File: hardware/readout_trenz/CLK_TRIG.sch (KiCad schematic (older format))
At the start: 11 parts, among them J2 Conn_Coaxial, J3 Conn_Coaxial, U1 NLSV4T244E, U2 LM6321N, U3 LM6321N

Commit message: _
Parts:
- removed U2, U3: LM6321N, Package_DIP:DIP-8_W7.62mm, symbol Amplifier_Buffer:LM6321N
- C1, C2: footprint (none) -> Capacitor_SMD:C_0603_1608Metric_Pad1.05x0.95mm_HandSolder
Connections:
- net labels removed: +3.3V
- wire segments 35 -> 29
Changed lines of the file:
@@
 Comment4 ""
 $EndDescr
-$Comp
-L Amplifier_Buffer:LM6321N U2
-U 1 1 60C7627C
-P 15300 2450
-F 0 "U2" H 15644 2496 50  0000 L CNN
-F 1 "LM6321N" H 15644 2405 50  0000 L CNN
-F 2 "Package_DIP:DIP-8_W7.62mm" H 15500 2050 50  0001 C CNN
-F 3 "http://www.electronica60norte.com/mwfls/pdf/LM6221.pdf" H 15300 2450 50  0001 C CNN
-	1    15300 2450
-	1    0    0    -1
-$EndComp
-$Comp
-L power:+3.3V #PWR08
-U 1 1 60C78956
-P 15200 1950
-F 0 "#PWR08" H 15200 1800 50  0001 C CNN
-F 1 "+3.3V" H 15215 2123 50  0000 C CNN
-F 2 "" H 15200 1950 50  0001 C CNN
-F 3 "" H 15200 1950 50  0001 C CNN
-	1    15200 1950
-	1    0    0    -1
-$EndComp
-Wire Wire Line
-	14000 2450 15000 2450
 Wire Wire Line
 	6850 3350 7750 3350
-Wire Wire Line
-	15200 2750 15200 2950
-Wire Wire Line
-	15200 2150 15200 1950
 Text HLabel 7750 3350 2    50   Output ~ 0
 CLOCK
@@
 	1    0    0    -1
 $EndComp
-$Comp
-L Amplifier_Buffer:LM6321N U3
-U 1 1 60C7B23A
-P 15300 4450
-F 0 "U3" H 15644 4496 50  0000 L CNN
-F 1 "LM6321N" H 15644 4405 50  0000 L CNN
-F 2 "Package_DIP:DIP-8_W7.62mm" H 15500 4050 50  0001 C CNN
-F 3 "http://www.electronica60norte.com/mwfls/pdf/LM6221.pdf" H 15300 4450 50  0001 C CNN
-	1    15300 4450
-	1    0    0    -1
-$EndComp
-$Comp
-L power:+3.3V #PWR010
-U 1 1 60C7B262
-P 15200 3950
-F 0 "#PWR010" H 15200 3800 50  0001 C CNN
-F 1 "+3.3V" H 15215 4123 50  0000 C CNN
-F 2 "" H 15200 3950 50  0001 C CNN
-F 3 "" H 15200 3950 50  0001 C CNN
-	1    15200 3950
-	1    0    0    -1
-$EndComp
 Wire Wire Line
 	4500 4200 4500 4500
@@
 	4700 4000 5500 4000
 Wire Wire Line
-	14000 4450 15000 4450
-Wire Wire Line
 	6850 3650 7750 3650
 Wire Wire Line
 	5500 4300 5500 4500
-Wire Wire Line
-	15200 4750 15200 4950
-Wire Wire Line
-	15200 4150 15200 3950
 Text HLabel 7750 3650 2    50   Output ~ 0
 TRIGGER
 Text Notes 4000 4000 0    50   ~ 0
 TRIGGER
-$Comp
-L power:GNDD #PWR09
-U 1 1 613569FF
-P 15200 2950
-F 0 "#PWR09" H 15200 2700 50  0001 C CNN
-F 1 "GNDD" H 15204 2795 50  0000 C CNN
-F 2 "" H 15200 2950 50  0001 C CNN
-F 3 "" H 15200 2950 50  0001 C CNN
-	1    15200 2950
-	1    0    0    -1
-$EndComp
 $Comp
 L power:GNDD #PWR03
@@
 F 3 "" H 5500 4500 50  0001 C CNN
 	1    5500 4500
-	1    0    0    -1
-$EndComp
-$Comp
-L power:GNDD #PWR011
-U 1 1 61358963
-P 15200 4950
-F 0 "#PWR011" H 15200 4700 50  0001 C CNN
-F 1 "GNDD" H 15204 4795 50  0000 C CNN
-F 2 "" H 15200 4950 50  0001 C CNN
-F 3 "" H 15200 4950 50  0001 C CNN
-	1    15200 4950
 	1    0    0    -1
 $EndComp
@@
 F 0 "C2" V 6900 2550 50  0000 L CNN
 F 1 "0.1uF" V 6800 2500 50  0000 L CNN
-F 2 "" H 6700 2600 50  0001 C CNN
+F 2 "Capacitor_SMD:C_0603_1608Metric_Pad1.05x0.95mm_HandSolder" H 6700 2600 50  0001 C CNN
 F 3 "~" H 6700 2600 50  0001 C CNN
 	1    6700 2600
@@
 F 0 "C1" V 6500 2550 50  0000 L CNN
 F 1 "0.1uF" V 6400 2500 50  0000 L CNN
-F 2 "" H 6300 2600 50  0001 C CNN
+F 2 "Capacitor_SMD:C_0603_1608Metric_Pad1.05x0.95mm_HandSolder" H 6300 2600 50  0001 C CNN
 F 3 "~" H 6300 2600 50  0001 C CNN
 	1    6300 2600

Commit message: Readout Preliminary Schematic Made
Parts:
- U1: footprint (none) -> Package_SO:TSSOP-14_4.4x5mm_P0.65mm; Item Cost (none) -> $1.97; MFN (none) -> NLSV4T244EDTR2G; Manufacturer (none) -> ON Semiconductors; Supplier (none) -> Digi-Key; Supplier P/N (none) -> NLSV4T244EDTR2GOSCT-ND
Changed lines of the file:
@@
 F 0 "U1" H 6500 3975 50  0000 C CNN
 F 1 "NLSV4T244E" H 6500 3884 50  0000 C CNN
-F 2 "" H 6500 3500 50  0001 C CNN
+F 2 "Package_SO:TSSOP-14_4.4x5mm_P0.65mm" H 6500 3500 50  0001 C CNN
 F 3 "https://www.onsemi.com/pdf/datasheet/nlsv4t244e-d.pdf" H 6500 3500 50  0001 C CNN
+F 4 "$1.97" H 6500 3500 50  0001 C CNN "Item Cost"
+F 5 "NLSV4T244EDTR2G" H 6500 3500 50  0001 C CNN "MFN"
+F 6 "ON Semiconductors" H 6500 3500 50  0001 C CNN "Manufacturer"
+F 7 "Digi-Key" H 6500 3500 50  0001 C CNN "Supplier"
+F 8 "NLSV4T244EDTR2GOSCT-ND" H 6500 3500 50  0001 C CNN "Supplier P/N"
 	1    6500 3500
 	1    0    0    -1

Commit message: Footprints Assigned
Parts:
- J2, J3: footprint (none) -> Readout_Board_Parts:lemo-EPB.00.250.NTN
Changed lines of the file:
@@
 F 0 "J3" H 4428 4238 50  0000 C CNN
 F 1 "Conn_Coaxial" H 4428 4147 50  0000 C CNN
-F 2 "" H 4500 4000 50  0001 C CNN
+F 2 "Readout_Board_Parts:lemo-EPB.00.250.NTN" H 4500 4000 50  0001 C CNN
 F 3 " ~" H 4500 4000 50  0001 C CNN
 	1    4500 4000
@@
 F 0 "J2" H 4428 3238 50  0000 C CNN
 F 1 "Conn_Coaxial" H 4428 3147 50  0000 C CNN
-F 2 "" H 4500 3000 50  0001 C CNN
+F 2 "Readout_Board_Parts:lemo-EPB.00.250.NTN" H 4500 3000 50  0001 C CNN
 F 3 " ~" H 4500 3000 50  0001 C CNN
 	1    4500 3000

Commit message: Starting Layout
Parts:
- C1, C2: Item Cost (none) -> $0.1; MFN (none) -> 885012206046; Manufacturer (none) -> Würth Elektronik; Supplier  (none) -> Digi-Key; Supplier P/N (none) -> 732-7965-1-ND
- U1: footprint Package_SO:TSSOP-14_4.4x5mm_P0.65mm -> Package_SO:SOIC-14_3.9x8.7mm_P1.27mm
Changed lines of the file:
@@
 F 0 "U1" H 6500 3975 50  0000 C CNN
 F 1 "NLSV4T244E" H 6500 3884 50  0000 C CNN
-F 2 "Package_SO:TSSOP-14_4.4x5mm_P0.65mm" H 6500 3500 50  0001 C CNN
+F 2 "Package_SO:SOIC-14_3.9x8.7mm_P1.27mm" H 6500 3500 50  0001 C CNN
 F 3 "https://www.onsemi.com/pdf/datasheet/nlsv4t244e-d.pdf" H 6500 3500 50  0001 C CNN
 F 4 "$1.97" H 6500 3500 50  0001 C CNN "Item Cost"
@@
 F 1 "0.1uF" V 6800 2500 50  0000 L CNN
 F 2 "Capacitor_SMD:C_0603_1608Metric_Pad1.05x0.95mm_HandSolder" H 6700 2600 50  0001 C CNN
-F 3 "~" H 6700 2600 50  0001 C CNN
+F 3 "https://www.we-online.de/katalog/datasheet/885012206046.pdf" H 6700 2600 50  0001 C CNN
+F 4 "$0.1" H 6700 2600 50  0001 C CNN "Item Cost"
+F 5 "885012206046" H 6700 2600 50  0001 C CNN "MFN"
+F 6 "Würth Elektronik" H 6700 2600 50  0001 C CNN "Manufacturer"
+F 7 "Digi-Key" H 6700 2600 50  0001 C CNN "Supplier "
+F 8 "732-7965-1-ND" H 6700 2600 50  0001 C CNN "Supplier P/N"
 	1    6700 2600
 	0    -1   -1   0
@@
 F 1 "0.1uF" V 6400 2500 50  0000 L CNN
 F 2 "Capacitor_SMD:C_0603_1608Metric_Pad1.05x0.95mm_HandSolder" H 6300 2600 50  0001 C CNN
-F 3 "~" H 6300 2600 50  0001 C CNN
+F 3 "https://www.we-online.de/katalog/datasheet/885012206046.pdf" H 6300 2600 50  0001 C CNN
+F 4 "$0.1" H 6300 2600 50  0001 C CNN "Item Cost"
+F 5 "885012206046" H 6300 2600 50  0001 C CNN "MFN"
+F 6 "Würth Elektronik" H 6300 2600 50  0001 C CNN "Manufacturer"
+F 7 "Digi-Key" H 6300 2600 50  0001 C CNN "Supplier "
+F 8 "732-7965-1-ND" H 6300 2600 50  0001 C CNN "Supplier P/N"
 	1    6300 2600
 	0    -1   -1   0

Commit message: -
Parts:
- J2, J3: footprint Readout_Board_Parts:lemo-EPB.00.250.NTN -> readout_trenz:lemo-EPB.00.250.NTN
- R1, R2: value 50 -> 56; Item Cost (none) -> $0.1; MFN (none) -> CRCW060356R0FKEAC; Manufacturer (none) -> Vishay Dale; Supplier  (none) -> Digi-Key; Supplier P/N (none) -> 541-5483-1-ND
- R3, R4: Item Cost (none) -> $0.01; MFN (none) -> CR0603AFX-1000ELF; Manufacturer (none) -> Bourns Inc.; Supplier  (none) -> Digi-Key; Supplier P/N (none) -> 118-CR0603AFX-1000ELFCT-ND
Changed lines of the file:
@@
 F 0 "J3" H 4428 4238 50  0000 C CNN
 F 1 "Conn_Coaxial" H 4428 4147 50  0000 C CNN
-F 2 "Readout_Board_Parts:lemo-EPB.00.250.NTN" H 4500 4000 50  0001 C CNN
+F 2 "readout_trenz:lemo-EPB.00.250.NTN" H 4500 4000 50  0001 C CNN
 F 3 " ~" H 4500 4000 50  0001 C CNN
 	1    4500 4000
@@
 P 5500 4150
 F 0 "R2" H 5570 4196 50  0000 L CNN
-F 1 "50" H 5570 4105 50  0000 L CNN
+F 1 "56" H 5570 4105 50  0000 L CNN
 F 2 "Resistor_SMD:R_0603_1608Metric_Pad1.05x0.95mm_HandSolder" V 5430 4150 50  0001 C CNN
-F 3 "~" H 5500 4150 50  0001 C CNN
+F 3 "https://www.vishay.com/docs/28773/crcwce3.pdf" H 5500 4150 50  0001 C CNN
+F 4 "$0.1" H 5500 4150 50  0001 C CNN "Item Cost"
+F 5 "CRCW060356R0FKEAC" H 5500 4150 50  0001 C CNN "MFN"
+F 6 "Vishay Dale" H 5500 4150 50  0001 C CNN "Manufacturer"
+F 7 "Digi-Key" H 5500 4150 50  0001 C CNN "Supplier "
+F 8 "541-5483-1-ND" H 5500 4150 50  0001 C CNN "Supplier P/N"
 	1    5500 4150
 	1    0    0    -1
@@
 P 5500 3150
 F 0 "R1" H 5570 3196 50  0000 L CNN
-F 1 "50" H 5570 3105 50  0000 L CNN
+F 1 "56" H 5570 3105 50  0000 L CNN
 F 2 "Resistor_SMD:R_0603_1608Metric_Pad1.05x0.95mm_HandSolder" V 5430 3150 50  0001 C CNN
-F 3 "~" H 5500 3150 50  0001 C CNN
+F 3 "https://www.vishay.com/docs/28773/crcwce3.pdf" H 5500 3150 50  0001 C CNN
+F 4 "$0.1" H 5500 3150 50  0001 C CNN "Item Cost"
+F 5 "CRCW060356R0FKEAC" H 5500 3150 50  0001 C CNN "MFN"
+F 6 "Vishay Dale" H 5500 3150 50  0001 C CNN "Manufacturer"
+F 7 "Digi-Key" H 5500 3150 50  0001 C CNN "Supplier "
+F 8 "541-5483-1-ND" H 5500 3150 50  0001 C CNN "Supplier P/N"
 	1    5500 3150
 	1    0    0    -1
@@
 F 0 "J2" H 4428 3238 50  0000 C CNN
 F 1 "Conn_Coaxial" H 4428 3147 50  0000 C CNN
-F 2 "Readout_Board_Parts:lemo-EPB.00.250.NTN" H 4500 3000 50  0001 C CNN
+F 2 "readout_trenz:lemo-EPB.00.250.NTN" H 4500 3000 50  0001 C CNN
 F 3 " ~" H 4500 3000 50  0001 C CNN
 	1    4500 3000
@@
 F 1 "100" H 6070 3755 50  0000 L CNN
 F 2 "Resistor_SMD:R_0603_1608Metric_Pad1.05x0.95mm_HandSolder" V 5930 3800 50  0001 C CNN
-F 3 "~" H 6000 3800 50  0001 C CNN
+F 3 "https://www.bourns.com/docs/product-datasheets/crxxxxa.pdf" H 6000 3800 50  0001 C CNN
+F 4 "$0.01" H 6000 3800 50  0001 C CNN "Item Cost"
+F 5 "CR0603AFX-1000ELF" H 6000 3800 50  0001 C CNN "MFN"
+F 6 "Bourns Inc." H 6000 3800 50  0001 C CNN "Manufacturer"
+F 7 "Digi-Key" H 6000 3800 50  0001 C CNN "Supplier "
+F 8 "118-CR0603AFX-1000ELFCT-ND" H 6000 3800 50  0001 C CNN "Supplier P/N"
 	1    6000 3800
 	-1   0    0    -1
@@
 F 1 "100" H 6070 3155 50  0000 L CNN
 F 2 "Resistor_SMD:R_0603_1608Metric_Pad1.05x0.95mm_HandSolder" V 5930 3200 50  0001 C CNN
-F 3 "~" H 6000 3200 50  0001 C CNN
+F 3 "https://www.bourns.com/docs/product-datasheets/crxxxxa.pdf" H 6000 3200 50  0001 C CNN
+F 4 "$0.01" H 6000 3200 50  0001 C CNN "Item Cost"
+F 5 "CR0603AFX-1000ELF" H 6000 3200 50  0001 C CNN "MFN"
+F 6 "Bourns Inc." H 6000 3200 50  0001 C CNN "Manufacturer"
+F 7 "Digi-Key" H 6000 3200 50  0001 C CNN "Supplier "
+F 8 "118-CR0603AFX-1000ELFCT-ND" H 6000 3200 50  0001 C CNN "Supplier P/N"
 	1    6000 3200
 	-1   0    0    -1

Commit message: On Layout
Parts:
- U1: footprint Package_SO:SOIC-14_3.9x8.7mm_P1.27mm -> Package_SO:TSSOP-14_4.4x5mm_P0.65mm; Supplier  (none) -> Digi-Key
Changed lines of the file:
@@
 F 0 "U1" H 6500 3975 50  0000 C CNN
 F 1 "NLSV4T244E" H 6500 3884 50  0000 C CNN
-F 2 "Package_SO:SOIC-14_3.9x8.7mm_P1.27mm" H 6500 3500 50  0001 C CNN
+F 2 "Package_SO:TSSOP-14_4.4x5mm_P0.65mm" H 6500 3500 50  0001 C CNN
 F 3 "https://www.onsemi.com/pdf/datasheet/nlsv4t244e-d.pdf" H 6500 3500 50  0001 C CNN
 F 4 "$1.97" H 6500 3500 50  0001 C CNN "Item Cost"
@@
 F 7 "Digi-Key" H 6500 3500 50  0001 C CNN "Supplier"
 F 8 "NLSV4T244EDTR2GOSCT-ND" H 6500 3500 50  0001 C CNN "Supplier P/N"
+F 9 "Digi-Key" H 6500 3500 50  0001 C CNN "Supplier "
 	1    6500 3500
 	1    0    0    -1

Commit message: Readout Layout Started
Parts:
- U1: Supplier Digi-Key -> (none)
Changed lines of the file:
@@
 F 5 "NLSV4T244EDTR2G" H 6500 3500 50  0001 C CNN "MFN"
 F 6 "ON Semiconductors" H 6500 3500 50  0001 C CNN "Manufacturer"
-F 7 "Digi-Key" H 6500 3500 50  0001 C CNN "Supplier"
+F 7 "" H 6500 3500 50  0001 C CNN "Supplier"
 F 8 "NLSV4T244EDTR2GOSCT-ND" H 6500 3500 50  0001 C CNN "Supplier P/N"
 F 9 "Digi-Key" H 6500 3500 50  0001 C CNN "Supplier "

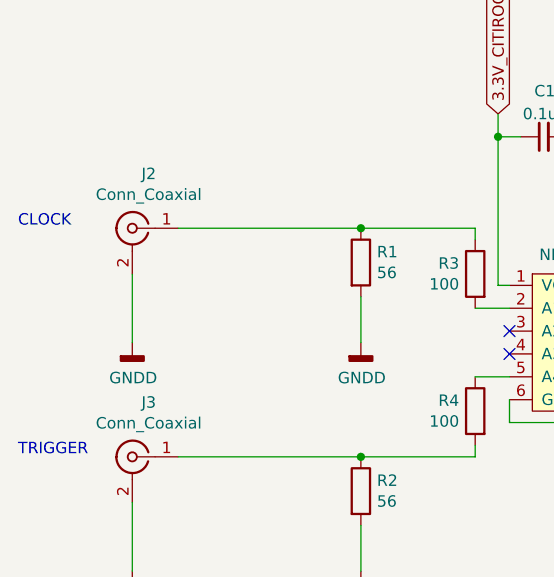
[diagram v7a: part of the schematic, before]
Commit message: Netlist errors fixed
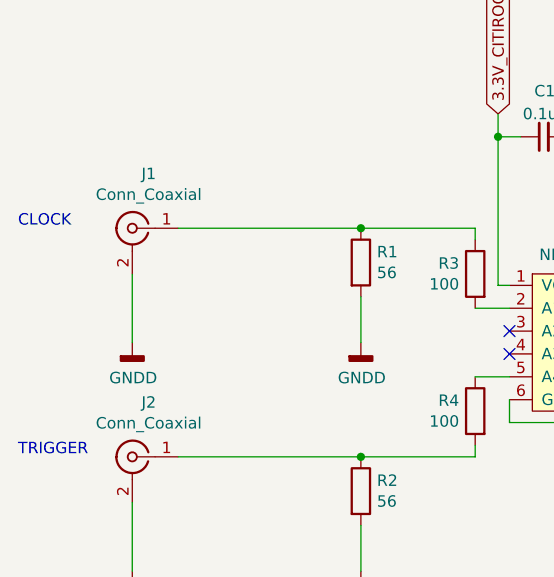
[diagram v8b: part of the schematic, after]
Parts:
- renumbered J2 to J1, J3 to J2
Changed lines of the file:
@@
 CLOCK\n
 $Comp
-L Connector:Conn_Coaxial J3
+L Connector:Conn_Coaxial J2
 U 1 1 60C7B226
 P 4500 4000
-F 0 "J3" H 4428 4238 50  0000 C CNN
+F 0 "J2" H 4428 4238 50  0000 C CNN
 F 1 "Conn_Coaxial" H 4428 4147 50  0000 C CNN
 F 2 "readout_trenz:lemo-EPB.00.250.NTN" H 4500 4000 50  0001 C CNN
@@
 TRIGGER
 $Comp
-L power:GNDD #PWR03
+L power:GNDD #PWR02
 U 1 1 6135894F
 P 4500 4500
-F 0 "#PWR03" H 4500 4250 50  0001 C CNN
+F 0 "#PWR02" H 4500 4250 50  0001 C CNN
 F 1 "GNDD" H 4504 4345 50  0000 C CNN
 F 2 "" H 4500 4500 50  0001 C CNN
@@
 $EndComp
 $Comp
-L power:GNDD #PWR05
+L power:GNDD #PWR04
 U 1 1 61358959
 P 5500 4500
-F 0 "#PWR05" H 5500 4250 50  0001 C CNN
+F 0 "#PWR04" H 5500 4250 50  0001 C CNN
 F 1 "GNDD" H 5504 4345 50  0000 C CNN
 F 2 "" H 5500 4500 50  0001 C CNN
@@
 	6850 3850 6850 3750
 $Comp
-L power:GNDD #PWR07
+L power:GNDD #PWR06
 U 1 1 61480617
 P 6500 3850
-F 0 "#PWR07" H 6500 3600 50  0001 C CNN
+F 0 "#PWR06" H 6500 3600 50  0001 C CNN
 F 1 "GNDD" H 6504 3695 50  0000 C CNN
 F 2 "" H 6500 3850 50  0001 C CNN
@@
 	6100 3250 6150 3250
 $Comp
-L power:GNDD #PWR04
+L power:GNDD #PWR03
 U 1 1 613558E3
 P 5500 3500
-F 0 "#PWR04" H 5500 3250 50  0001 C CNN
+F 0 "#PWR03" H 5500 3250 50  0001 C CNN
 F 1 "GNDD" H 5504 3345 50  0000 C CNN
 F 2 "" H 5500 3500 50  0001 C CNN
@@
 $EndComp
 $Comp
-L power:GNDD #PWR02
+L power:GNDD #PWR01
 U 1 1 6135534F
 P 4500 3500
-F 0 "#PWR02" H 4500 3250 50  0001 C CNN
+F 0 "#PWR01" H 4500 3250 50  0001 C CNN
 F 1 "GNDD" H 4504 3345 50  0000 C CNN
 F 2 "" H 4500 3500 50  0001 C CNN
@@
 $EndComp
 $Comp
-L Connector:Conn_Coaxial J2
+L Connector:Conn_Coaxial J1
 U 1 1 60C74CEF
 P 4500 3000
-F 0 "J2" H 4428 3238 50  0000 C CNN
+F 0 "J1" H 4428 3238 50  0000 C CNN
 F 1 "Conn_Coaxial" H 4428 3147 50  0000 C CNN
 F 2 "readout_trenz:lemo-EPB.00.250.NTN" H 4500 3000 50  0001 C CNN
@@
 AR Path="/60BB4C00/621A5295" Ref="#PWR?"  Part="1"
 AR Path="/60BB4A14/621A5295" Ref="#PWR?"  Part="1"
-AR Path="/60C74A7C/621A5295" Ref="#PWR06"  Part="1"
-F 0 "#PWR06" H 6500 2450 50  0001 C CNN
+AR Path="/60C74A7C/621A5295" Ref="#PWR05"  Part="1"
+F 0 "#PWR05" H 6500 2450 50  0001 C CNN
 F 1 "GNDD" H 6504 2545 50  0000 C CNN
 F 2 "" H 6500 2700 50  0001 C CNN
